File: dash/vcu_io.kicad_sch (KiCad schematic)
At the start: 56 parts, among them J3 M80-5102042, Q2 XP262N7002TR-G, Q3 XP262N7002TR-G, Q4 XP262N7002TR-G, Q5 XP262N7002TR-G, U30 TCAN3404-Q1, U42 TCAN3404-Q1

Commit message: routing
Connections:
- net CAN1_RX: now also U30.4 (RXD); no longer U42.4 (RXD)
- net CAN1_TX: now also U30.1 (TXD); no longer U42.1 (TXD)
- net CAN2_RX: now also U42.4 (RXD); no longer U30.4 (RXD)
- net CAN2_TX: now also U42.1 (TXD); no longer U30.1 (TXD)
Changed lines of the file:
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@@
 	(hierarchical_label "CAN1_RX"
+		(shape output)
+		(at 34.29 138.43 180)
+		(effects
+			(font
+				(size 1.27 1.27)
+			)
+			(justify right)
+		)
+	)
+	(hierarchical_label "CAN2_RX"
 		(shape output)
 		(at 34.29 49.53 180)
@@
 		)
 	)
-	(hierarchical_label "CAN2_RX"
-		(shape output)
-		(at 34.29 138.43 180)
+	(hierarchical_label "CAN1_TX"
+		(shape input)
+		(at 34.29 135.89 180)
 		(effects
 			(font
@@
 	(hierarchical_label "CAN2_TX"
 		(shape input)
-		(at 34.29 135.89 180)
-		(effects
-			(font
-				(size 1.27 1.27)
-			)
-			(justify right)
-		)
-	)
-	(hierarchical_label "CAN1_TX"
-		(shape input)
 		(at 34.29 46.99 180)

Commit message: Changed Inductors
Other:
- moved on the sheet: J3

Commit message: Beep Boop
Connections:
- net TSAL.DASH.EXC: now also R17.1
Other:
- moved on the sheet: J3

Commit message: Lots of routing stuff and updating connectors
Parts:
- removed Q4, Q5: XP262N7002TR-G, Package_TO_SOT_SMD:SOT-23, symbol Device:Q_NMOS_GSD
- removed R15, R16, R17, R18, R19, R20: 1K, Resistor_SMD:R_0603_1608Metric, symbol Device:R
- removed R21, R23: 10k, Resistor_SMD:R_0603_1608Metric, symbol Device:R
- removed R22: 10k, Resistor_SMD:R_0603_1608Metric, symbol Device:R_Small
- removed R24, R25: 0, Resistor_SMD:R_0603_1608Metric, symbol Device:R_Small
- removed SP1, SP10, SP11, SP12, SP13, SP14, SP15, SP16, SP17, SP18, SP19, SP2, SP20, SP21, SP22, SP23, SP24, SP3, SP4, SP5, SP6, SP7, SP8, SP9: Solder Pad, TestPoint:TestPoint_Pad_D2.0mm, symbol Connector:TestPoint
- added J10, J11, J12: Conn_02x02_Top_Bottom, Connector_Molex:Molex_Micro-Fit_3.0_43045-0412_2x02_P3.00mm_Vertical, symbol Connector_Generic:Conn_02x02_Top_Bottom
- added J7, J8, J9: Conn_02x01, Connector_Molex:Molex_Micro-Fit_3.0_43045-0212_2x01_P3.00mm_Vertical, symbol Connector_Generic:Conn_02x01
- added Q6, Q7: XP262N7002TR-G, Package_TO_SOT_SMD:SOT-23, symbol Device:Q_NMOS_GSD
- added R28, R56: 10k, Resistor_SMD:R_0603_1608Metric, symbol Device:R
- added R63, R69, R70, R71: 220R, Resistor_SMD:R_0603_1608Metric, symbol Device:R
- added R72: 1K, Resistor_SMD:R_0603_1608Metric, symbol Device:R
- added R73: 330R, Resistor_SMD:R_0603_1608Metric, symbol Device:R
- U30, U42: footprint Package_SO:SOIC-8_3.9x4.9mm_P1.27mm -> Package_TO_SOT_SMD:SOT-23-8_Handsoldering
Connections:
- net LED_IMD_FAULT is gone; now on net AMS.LED.SIG: Q2.1 (G), R13.1
- net AMS.LED.SIG: now also J3.3 (Pin_3); no longer J3.19 (Pin_19)
- net CAN.C+: now also J3.17 (Pin_17), J3.7 (Pin_7); no longer J3.3 (Pin_3), J3.5 (Pin_5)
- net CAN.C-: now also J3.18 (Pin_18), J3.8 (Pin_8); no longer J3.4 (Pin_4), J3.6 (Pin_6)
- net CAN.F+: now also J3.19 (Pin_19); no longer J3.7 (Pin_7)
- net CAN.F-: now also J3.20 (Pin_20); no longer J3.8 (Pin_8)
- net GND: now also J3.11 (Pin_11), Q6.2 (S), Q7.2 (S), R28.2; no longer J3.20 (Pin_20)
- net IMD.LED.SIG: now also J3.13 (Pin_13), Q6.1 (G), R28.1; no longer J3.18 (Pin_18)
- net R2D.BUTTON.GND: now also J3.4 (Pin_4), J11.3 (Pin_3); no longer J3.13 (Pin_13)
- net R2D.LED.GND: now also J11.4 (Pin_4)
- net SPARE.BUTTON.GND: now also J3.6 (Pin_6), J12.3 (Pin_3); no longer J3.15 (Pin_15)
- net SPARE.LED.GND: now also J12.4 (Pin_4)
- net TS.ON.BUTTON.GND: now also J3.5 (Pin_5), J10.3 (Pin_3); no longer J3.11 (Pin_11)
- net TS.ON.LED.GND: now also J3.15 (Pin_15), J10.4 (Pin_4); no longer J3.12 (Pin_12)
- net TSAL.DASH.EXC: now also R73.1
- net TSAL.GREEN.DASH.LED.GND: now also J3.12 (Pin_12), J9.2 (Pin_2); no longer J3.17 (Pin_17)
- net AMS_LED_SCS: now reaches Q3.3 (D)
- net AMS_LED_SCS: now also J7.2 (Pin_2)
- net +12V renamed +GLV_PROT
- net +GLV_PROT: now also J10.1 (Pin_1), J11.1 (Pin_1), J12.1 (Pin_1), R56.1, R63.1, R69.1, R70.1, R71.1, R72.1
- new net: J12.2 (Pin_2), R72.2
- new net: J10.2 (Pin_2), R70.2
- new net: J7.1 (Pin_1), R63.2
- new net: J8.1 (Pin_1), R69.2
- new net: J9.1 (Pin_1), R73.2
- new net: J11.2 (Pin_2), R71.2
- new net: Q6.3 (D), Q7.1 (G), R56.2
- new net IMD_LED_SCS: J8.2 (Pin_2), Q7.3 (D)
- no-connect marks 8 -> 2
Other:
- note removed: "AMS/IMD: 220R TS_ON: 330R R2D: 220R"
- note removed: "BUTTON CONNECTION"
- note removed: "LED CONNECTION"
- note removed: "SCS quirk. If the wire is grounded / disconnected, we want the LED to come on, but the already-built circuits think they're driving the LEDs themselves. The logic here is: If input is low, drive LED, else LED off."
- note removed: "Solder Pads"
- note removed: "TODO: Red LEDs need lower resistance to be visible"
- note removed: "This button isn't used"
- note removed: "VCU CONNECTION"
- moved on the sheet: Q2, Q3, R13, R14

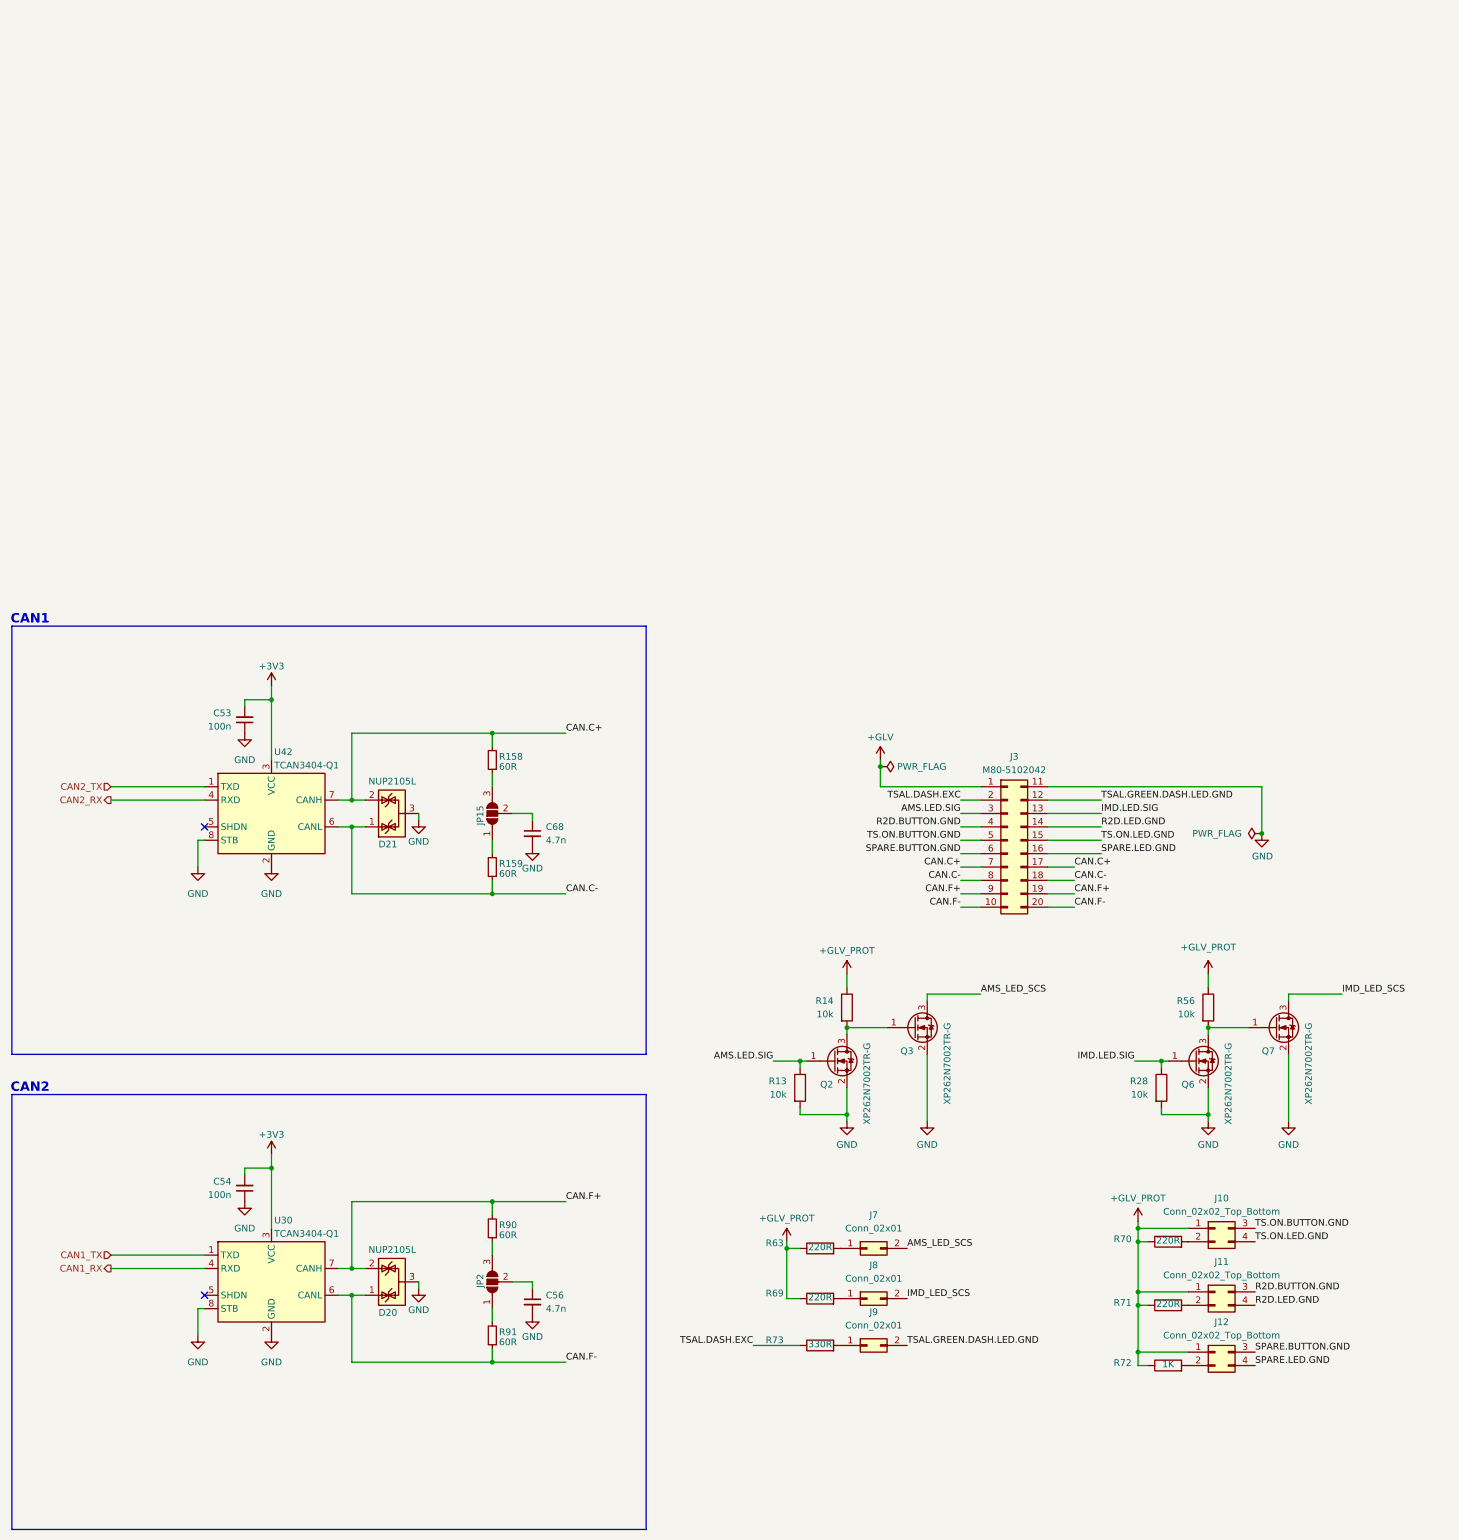
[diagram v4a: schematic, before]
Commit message: Reassigned footprints among other changes
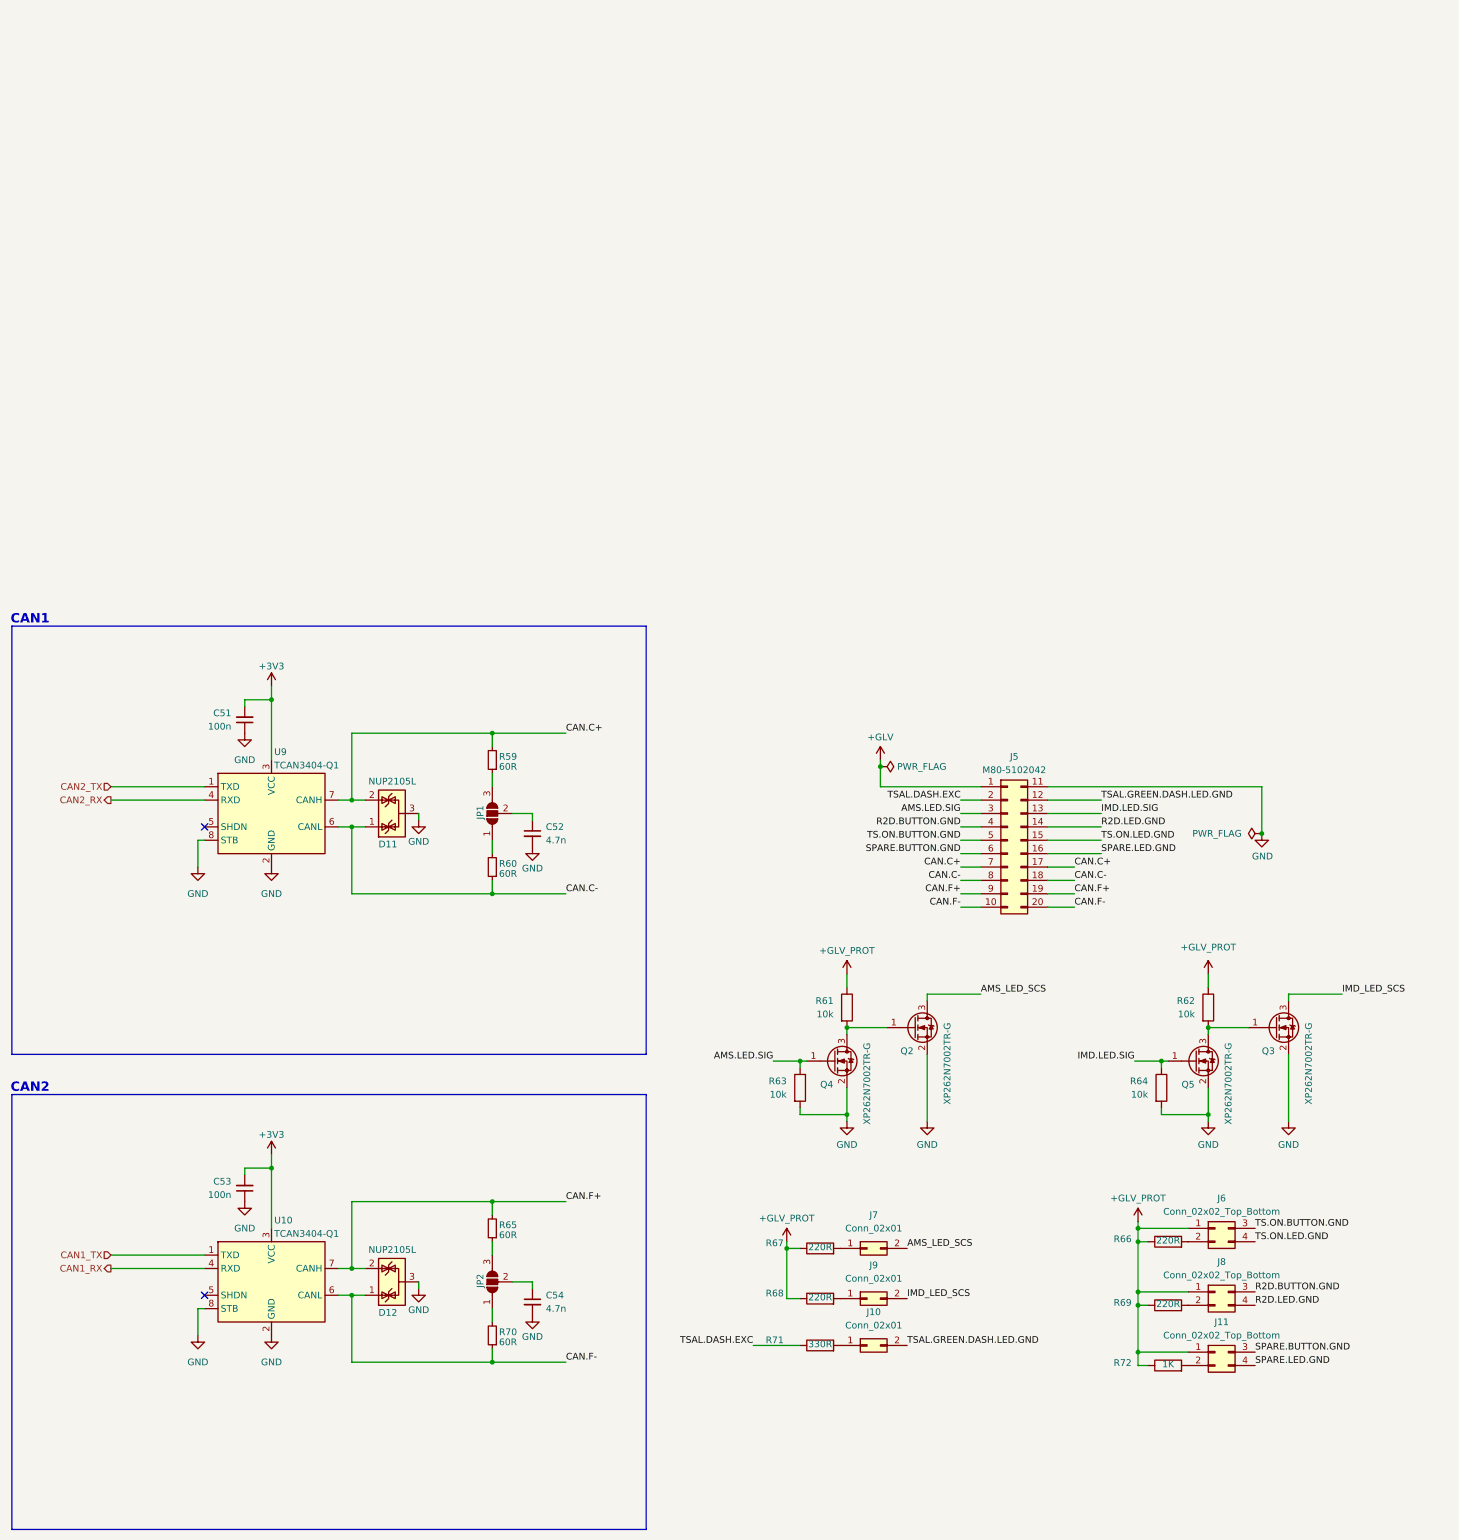
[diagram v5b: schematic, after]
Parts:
- renumbered C53 to C51, C68 to C52, C54 to C53, C56 to C54, D21 to D11, D20 to D12, J9 to J10, J12 to J11, J3 to J5, J10 to J6, J11 to J8, J8 to J9, JP15 to JP1, Q3 to Q2, Q7 to Q3, Q2 to Q4, Q6 to Q5, R158 to R59, R159 to R60, R14 to R61, R56 to R62, R13 to R63, R28 to R64, R90 to R65, R70 to R66, R63 to R67, R69 to R68, R71 to R69, R91 to R70, R73 to R71, U30 to U10, U42 to U9

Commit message: finishing
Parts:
- added R73, R74, R75: 10K, Resistor_SMD:R_0603_1608Metric, symbol Device:R
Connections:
- net GND: now also R73.1, R74.1, R75.1
- net R2D.BUTTON.GND: now also R74.2
- net SPARE.BUTTON.GND: now also R75.2
- net TS.ON.BUTTON.GND: now also R73.2
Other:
- moved on the sheet: J10, J11, J6, J7, J8, J9, R66, R67, R68, R69, R71, R72

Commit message: Adding 3d models, changing resistors
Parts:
- R66, R67, R68, R69, R71, R72: footprint Resistor_SMD:R_0603_1608Metric -> Resistor_SMD:R_0805_2012Metric
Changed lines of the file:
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@@
 			)
 		)
-		(property "Footprint" "Resistor_SMD:R_0603_1608Metric"
+		(property "Footprint" "Resistor_SMD:R_0805_2012Metric"
 			(at 220.345 135.128 90)
 			(effects
@@
 			)
 		)
-		(property "Footprint" "Resistor_SMD:R_0603_1608Metric"
+		(property "Footprint" "Resistor_SMD:R_0805_2012Metric"
 			(at 163.83 144.653 90)
 			(effects
@@
 			)
 		)
-		(property "Footprint" "Resistor_SMD:R_0603_1608Metric"
+		(property "Footprint" "Resistor_SMD:R_0805_2012Metric"
 			(at 163.83 153.543 90)
 			(effects
@@
 			)
 		)
-		(property "Footprint" "Resistor_SMD:R_0603_1608Metric"
+		(property "Footprint" "Resistor_SMD:R_0805_2012Metric"
 			(at 220.345 147.193 90)
 			(effects
@@
 			)
 		)
-		(property "Footprint" "Resistor_SMD:R_0603_1608Metric"
+		(property "Footprint" "Resistor_SMD:R_0805_2012Metric"
 			(at 163.83 135.128 90)
 			(effects
@@
 			)
 		)
-		(property "Footprint" "Resistor_SMD:R_0603_1608Metric"
+		(property "Footprint" "Resistor_SMD:R_0805_2012Metric"
 			(at 220.345 158.623 90)
 			(effects

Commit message: Adding silkscreen, cleaning up DRC
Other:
- moved on the sheet: J10, J11, J6, J8, J9, R66, R68, R69, R71, R72, R73, R74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
